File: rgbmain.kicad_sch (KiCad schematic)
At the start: 6 parts, among them J1 Conn_01x10_Pin, J2 Conn_01x10_Pin, J3 Conn_01x09_Pin, J4 Conn_01x09_Pin, J5 Conn_01x06_Pin, J6 Conn_01x06_Pin

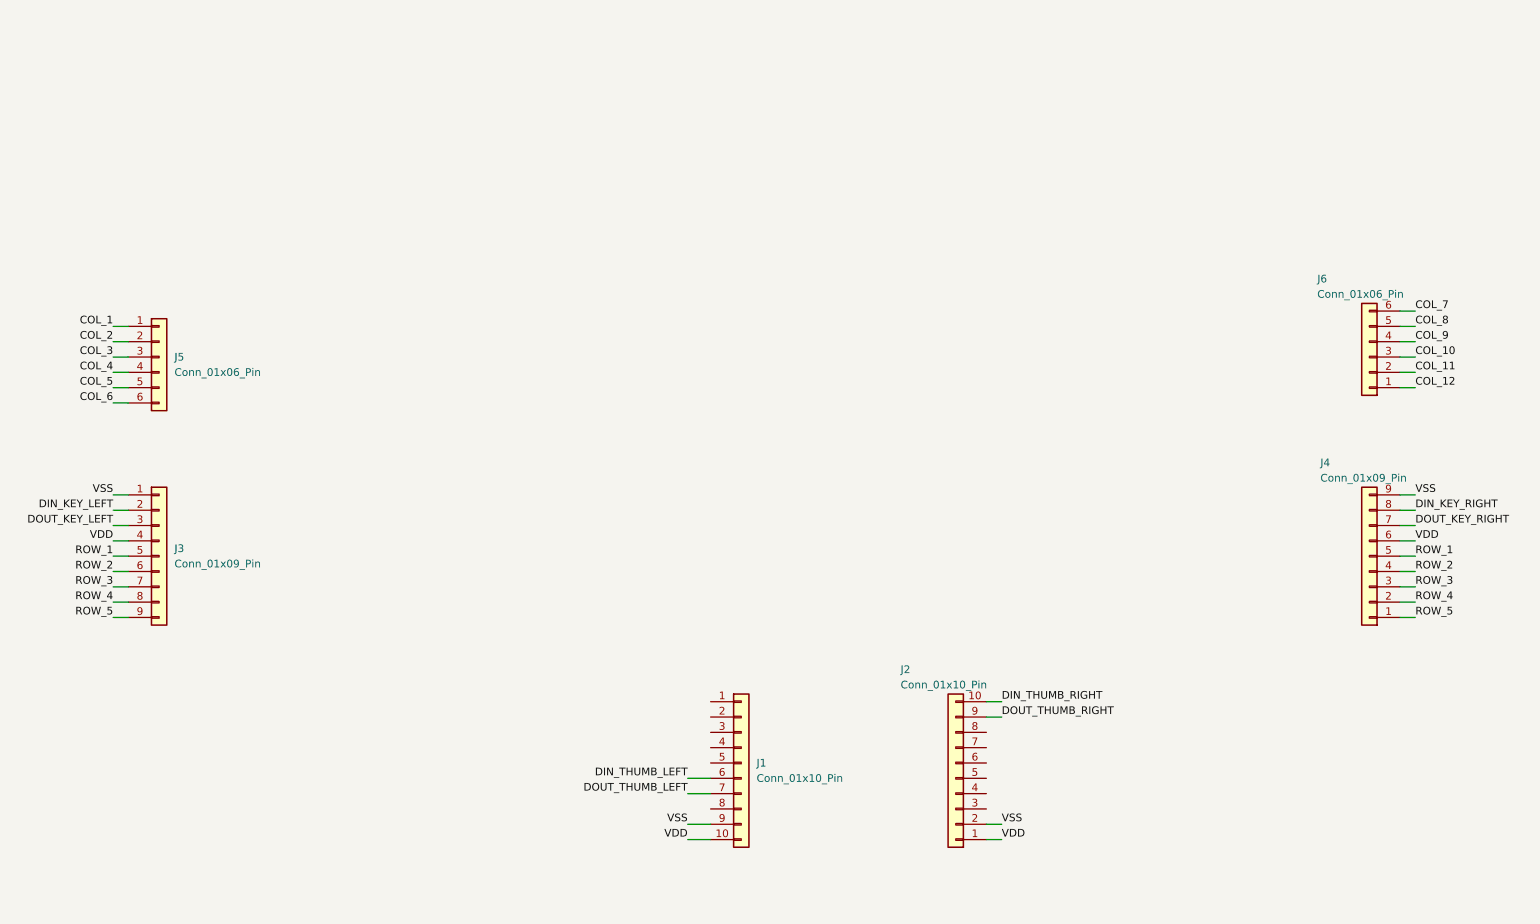
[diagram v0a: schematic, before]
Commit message: right side connectors were rotated incorrectly
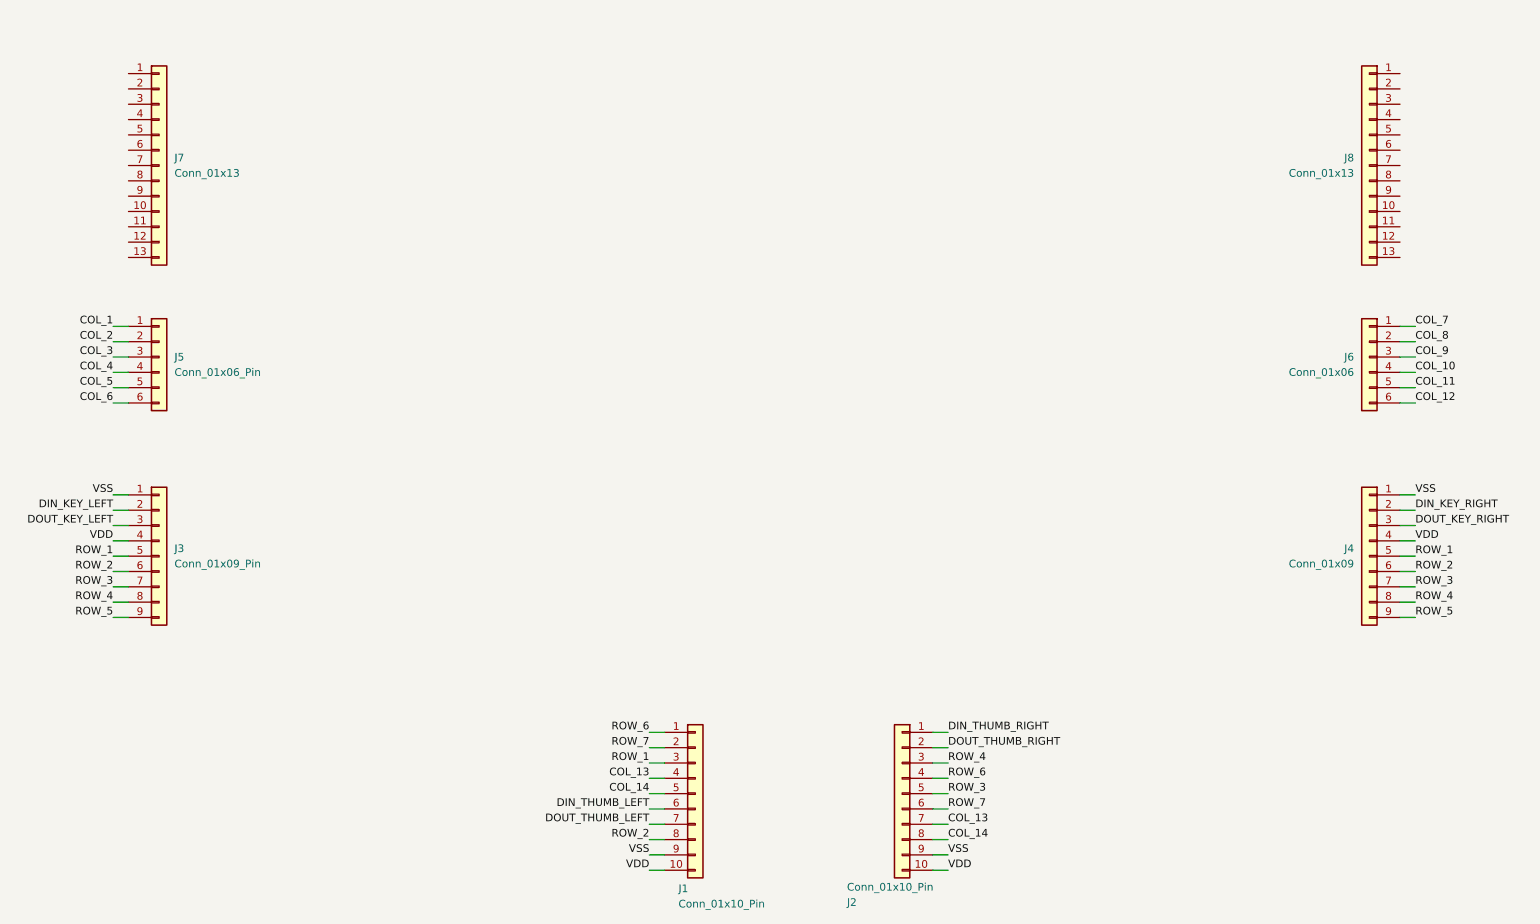
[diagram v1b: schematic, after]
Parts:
- added J7, J8: Conn_01x13, symbol Connector_Generic:Conn_01x13
- J4: value Conn_01x09_Pin -> Conn_01x09
- J6: value Conn_01x06_Pin -> Conn_01x06
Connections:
- net COL_10: now also J6.4 (Pin_4); no longer J6.3 (Pin_3)
- net COL_11: now also J6.5 (Pin_5); no longer J6.2 (Pin_2)
- net COL_12: now also J6.6 (Pin_6); no longer J6.1 (Pin_1)
- net COL_7: now also J6.1 (Pin_1); no longer J6.6 (Pin_6)
- net COL_8: now also J6.2 (Pin_2); no longer J6.5 (Pin_5)
- net COL_9: now also J6.3 (Pin_3); no longer J6.4 (Pin_4)
- net DIN_KEY_RIGHT: now also J4.2 (Pin_2); no longer J4.8 (Pin_8)
- net DIN_THUMB_RIGHT: now also J2.1 (Pin_1); no longer J2.10 (Pin_10)
- net DOUT_KEY_RIGHT: now also J4.3 (Pin_3); no longer J4.7 (Pin_7)
- net DOUT_THUMB_RIGHT: now also J2.2 (Pin_2); no longer J2.9 (Pin_9)
- net ROW_1: now also J1.3 (Pin_3)
- net ROW_2: now also J1.8 (Pin_8), J4.6 (Pin_6); no longer J4.4 (Pin_4)
- net ROW_3: now also J2.5 (Pin_5), J4.7 (Pin_7); no longer J4.3 (Pin_3)
- net ROW_4: now also J2.3 (Pin_3), J4.8 (Pin_8); no longer J4.2 (Pin_2)
- net ROW_5: now also J4.9 (Pin_9); no longer J4.1 (Pin_1)
- net VDD: now also J2.10 (Pin_10), J4.4 (Pin_4); no longer J2.1 (Pin_1), J4.6 (Pin_6)
- net VSS: now also J2.9 (Pin_9), J4.1 (Pin_1); no longer J2.2 (Pin_2), J4.9 (Pin_9)
- net ROW_6: now reaches J2.4 (Pin_4)
- net ROW_6: now also J1.1 (Pin_1)
- net ROW_7: now reaches J2.6 (Pin_6)
- net ROW_7: now also J1.2 (Pin_2)
- net COL_13: now reaches J2.7 (Pin_7)
- net COL_13: now also J1.4 (Pin_4)
- net COL_14: now reaches J2.8 (Pin_8)
- net COL_14: now also J1.5 (Pin_5)
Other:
- moved on the sheet: J1, J2

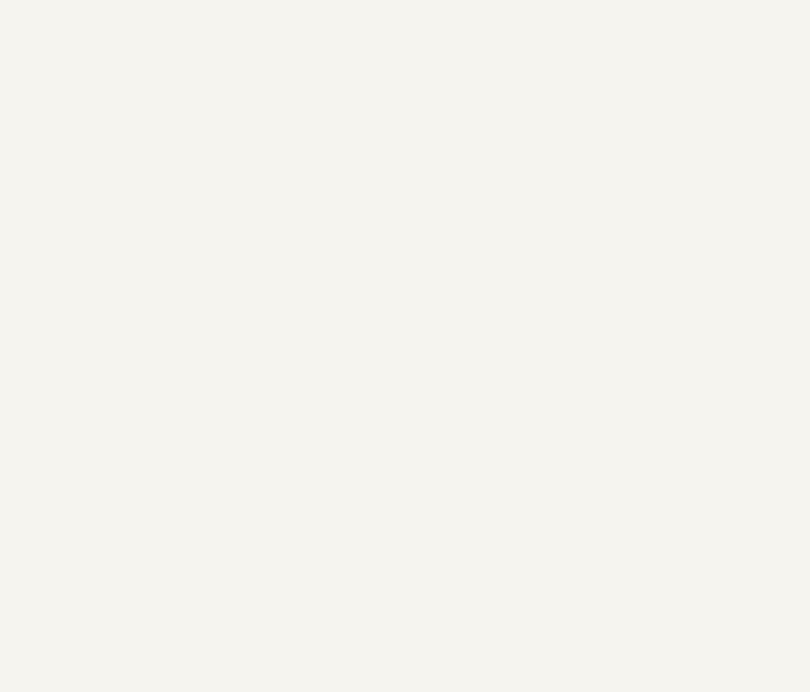
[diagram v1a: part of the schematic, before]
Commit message: symbol for Elite-Pi added
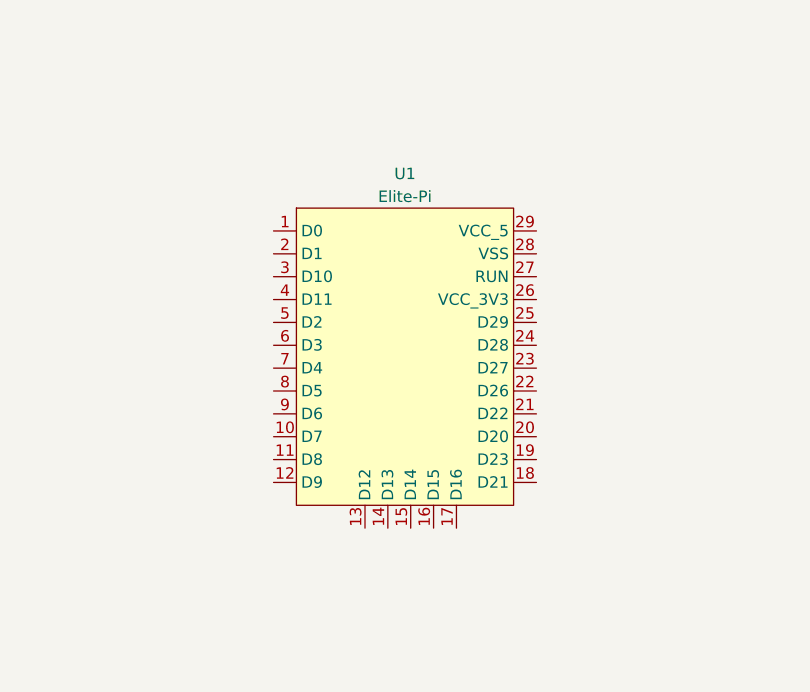
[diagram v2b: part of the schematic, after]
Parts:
- added U1: Elite-Pi, symbol rgbmain:Elite-PI
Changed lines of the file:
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@@
+	)
+	(symbol
+		(lib_id "rgbmain:Elite-PI")
+		(at 144.78 62.23 0)
+		(unit 1)
+		(exclude_from_sim no)
+		(in_bom yes)
+		(on_board yes)
+		(dnp no)
+		(fields_autoplaced yes)
+		(property "Reference" "U1"
+			(at 144.145 43.18 0)
+			(effects
+				(font
+					(size 1.27 1.27)
+				)
+			)
+		)
+		(property "Value" "Elite-Pi"
+			(at 144.145 45.72 0)
+			(effects
+				(font
+					(size 1.27 1.27)
+				)
+			)
+		)
+		(property "Footprint" ""
+			(at 144.78 62.23 0)
+			(effects
+				(font
+					(size 1.27 1.27)
+				)
+			)
+		)
+		(property "Datasheet" "https://docs.keeb.io/elite-pi-guide"
+			(at 144.526 97.536 0)
+			(effects
+				(font
+					(size 1.27 1.27)
+				)
+				(hide yes)
+			)
+		)
+		(property "Description" "Elite-Pi is a microcontroller based on the RP2040 designed for custom keyboards."
+			(at 144.526 95.504 0)
+			(effects
+				(font
+					(size 1.27 1.27)
+				)
+				(hide yes)
+			)
+		)
+		(pin "19"
+		)
+		(pin "15"
+		)
+		(pin "17"
+		)
+		(pin "22"
+		)
+		(pin "21"
+		)
+		(pin "12"
+		)
+		(pin "7"
+		)
+		(pin "18"
+		)
+		(pin "5"
+		)
+		(pin "16"
+		)
+		(pin "13"
+		)
+		(pin "8"
+		)
+		(pin "26"
+		)
+		(pin "14"
+		)
+		(pin "24"
+		)
+		(pin "10"
+		)
+		(pin "6"
+		)
+		(pin "3"
+		)
+		(pin "20"
+		)
+		(pin "23"
+		)
+		(pin "29"
+		)
+		(pin "9"
+		)
+		(pin "25"
+		)
+		(pin "1"
+		)
+		(pin "4"
+		)
+		(pin "11"
+		)
+		(pin "27"
+		)
+		(pin "28"
+		)
+		(pin "2"
+		)
+		(instances
+			(project ""
+				(path "/24ca604d-a7a4-46c7-a288-45b7cfc45cc9"
+					(reference "U1")
+					(unit 1)
+				)
+			)
+		)
 	)
 	(symbol

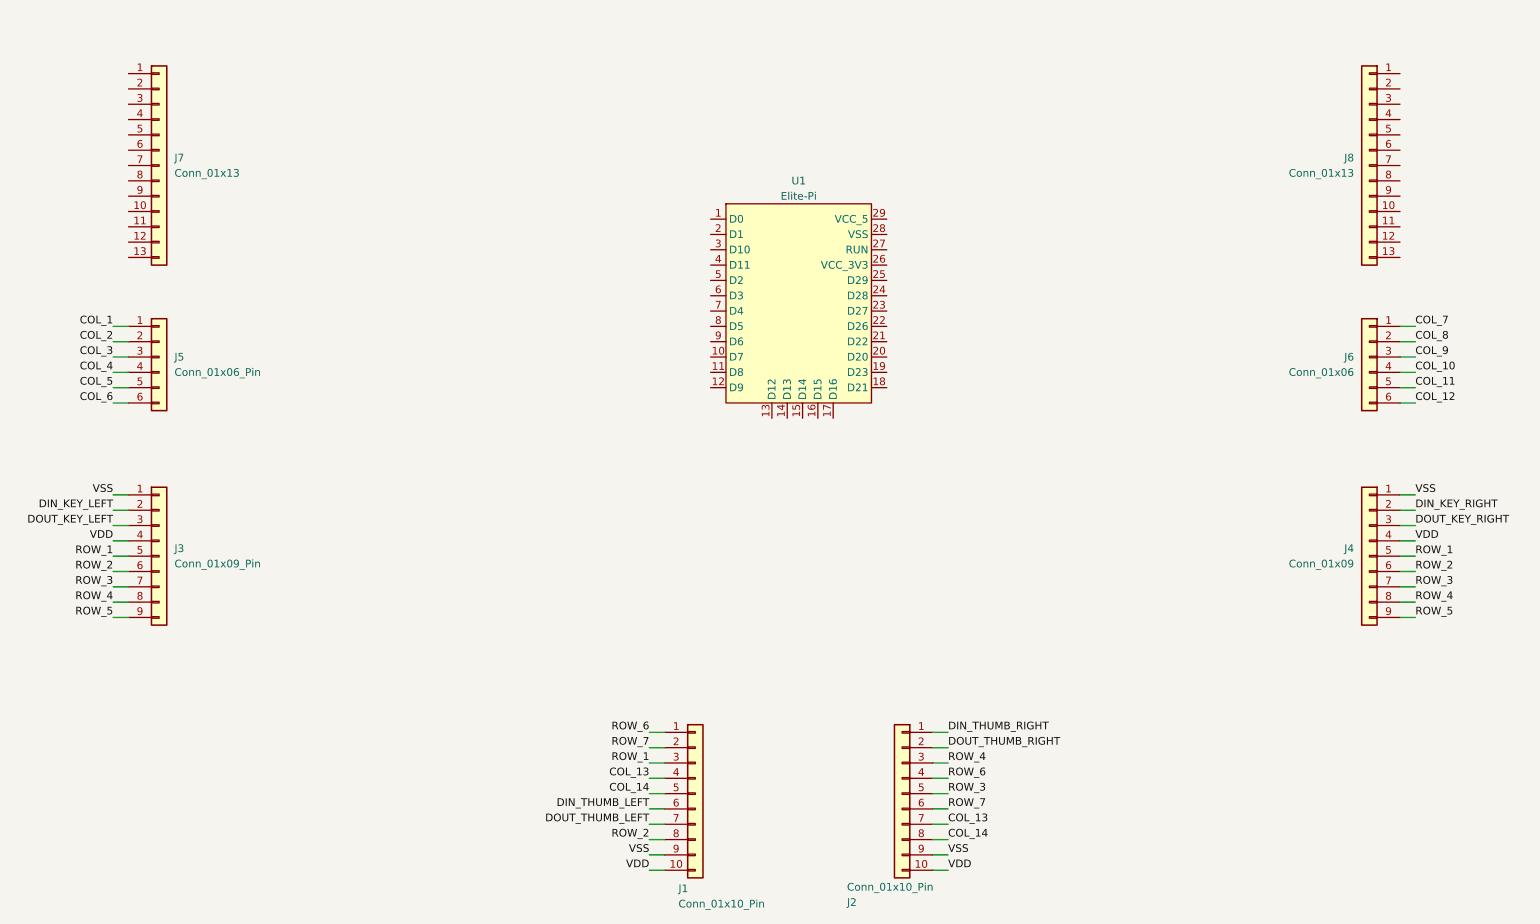
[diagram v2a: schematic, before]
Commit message: wire mcu up
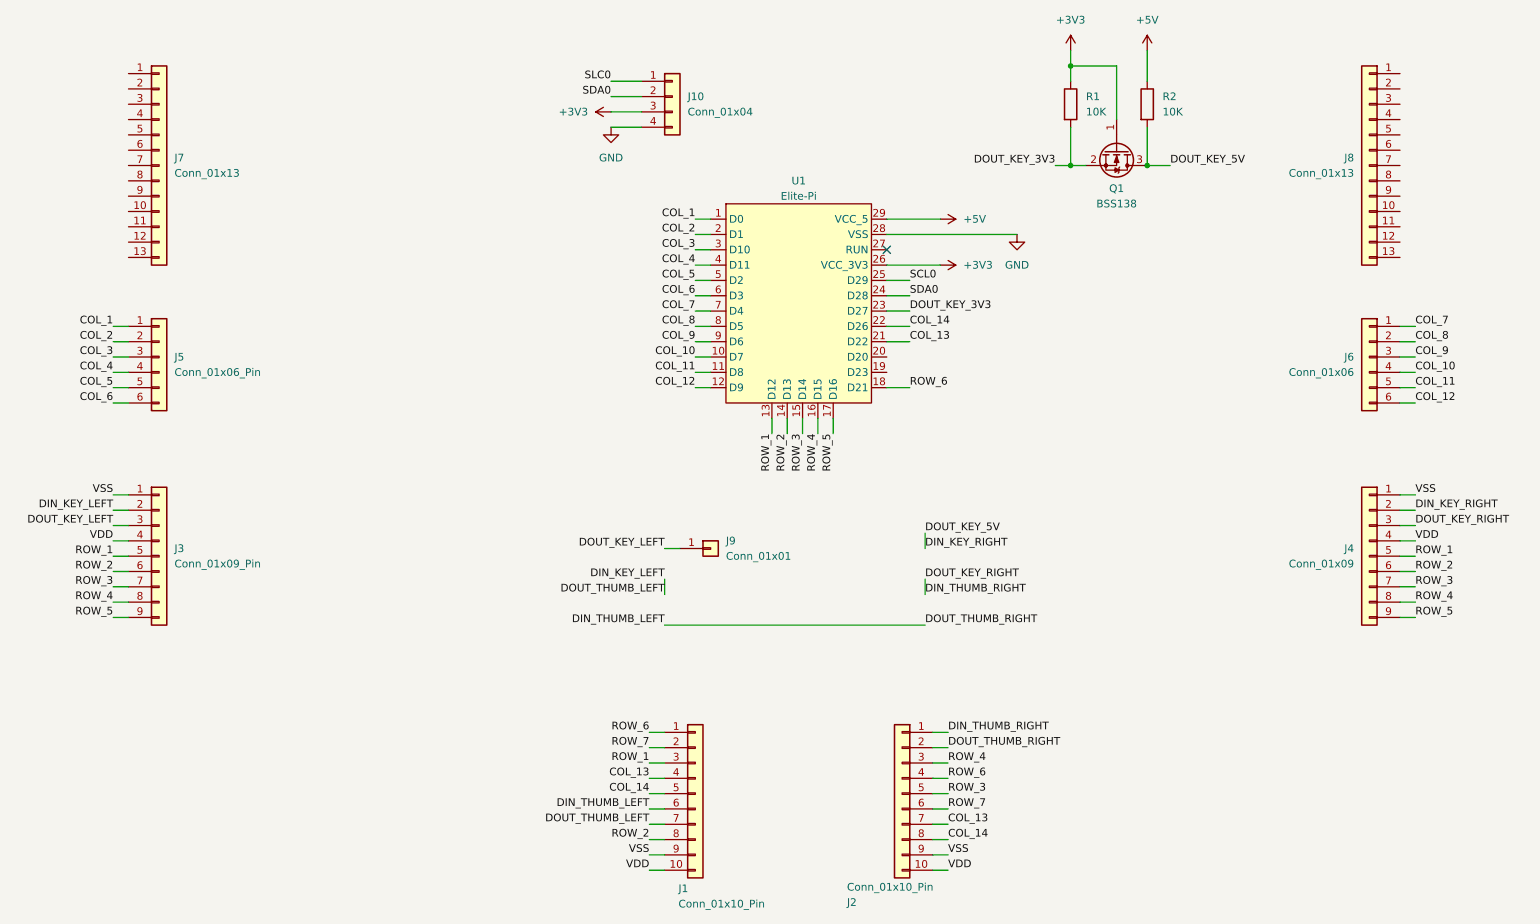
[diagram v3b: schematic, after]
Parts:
- added J10: Conn_01x04, symbol Connector_Generic:Conn_01x04
- added J9: Conn_01x01, symbol Connector_Generic:Conn_01x01
- added Q1: BSS138, Package_TO_SOT_SMD:SOT-23, symbol Transistor_FET:BSS138
- added R1, R2: 10K, symbol Device:R
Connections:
- net DOUT_KEY_RIGHT is gone; now on net DIN_THUMB_RIGHT: J4.3 (Pin_3)
- net DOUT_THUMB_LEFT is gone; now on net DIN_KEY_LEFT: J1.7 (Pin_7)
- net DOUT_THUMB_RIGHT is gone; now on net DIN_THUMB_LEFT: J2.2 (Pin_2)
- net COL_1: now also U1.1 (D0)
- net COL_10: now also U1.10 (D7)
- net COL_11: now also U1.11 (D8)
- net COL_12: now also U1.12 (D9)
- net COL_13: now also U1.21 (D22)
- net COL_14: now also U1.22 (D26)
- net COL_2: now also U1.2 (D1)
- net COL_3: now also U1.3 (D10)
- net COL_4: now also U1.4 (D11)
- net COL_5: now also U1.5 (D2)
- net COL_6: now also U1.6 (D3)
- net COL_7: now also U1.7 (D4)
- net COL_8: now also U1.8 (D5)
- net COL_9: now also U1.9 (D6)
- net DIN_KEY_RIGHT: now also Q1.3 (D), R2.2
- net DOUT_KEY_LEFT: now also J9.1 (Pin_1)
- net ROW_1: now also U1.13 (D12)
- net ROW_2: now also U1.14 (D13)
- net ROW_3: now also U1.15 (D14)
- net ROW_4: now also U1.16 (D15)
- net ROW_5: now also U1.17 (D16)
- net ROW_6: now also U1.18 (D21)
- net DOUT_KEY_3V3: now reaches U1.23 (D27)
- net DOUT_KEY_3V3: now also Q1.2 (S), R1.2
- net SDA0: now reaches U1.24 (D28)
- net SDA0: now also J10.2 (Pin_2)
- net SCL0: now reaches U1.25 (D29)
- net +3V3: now reaches U1.26 (VCC_3V3)
- net +3V3: now also J10.3 (Pin_3), Q1.1 (G), R1.1
- net GND: now reaches U1.28 (VSS)
- net GND: now also J10.4 (Pin_4)
- net +5V: now reaches U1.29 (VCC_5)
- net +5V: now also R2.1
- new net SLC0: J10.1 (Pin_1)
- no-connect marks 0 -> 1

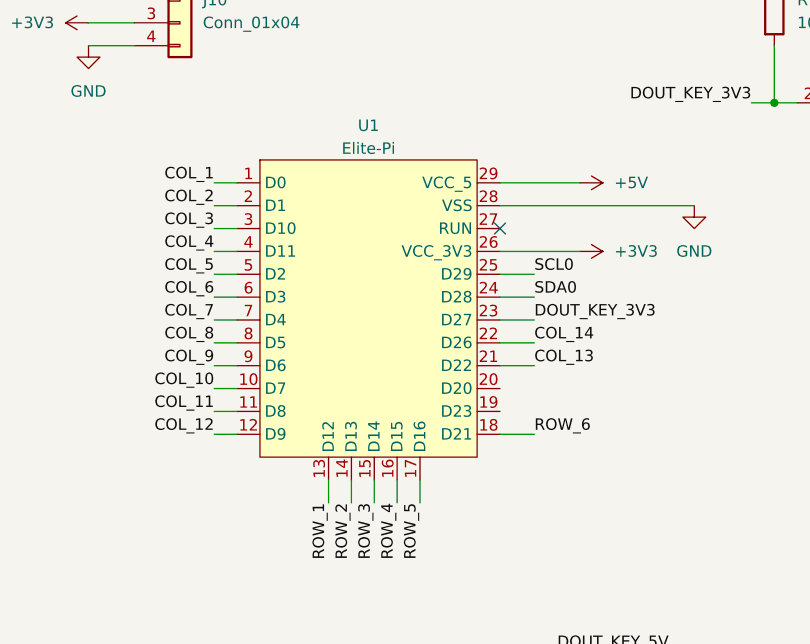
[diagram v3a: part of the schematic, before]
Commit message: changed number to match footprint
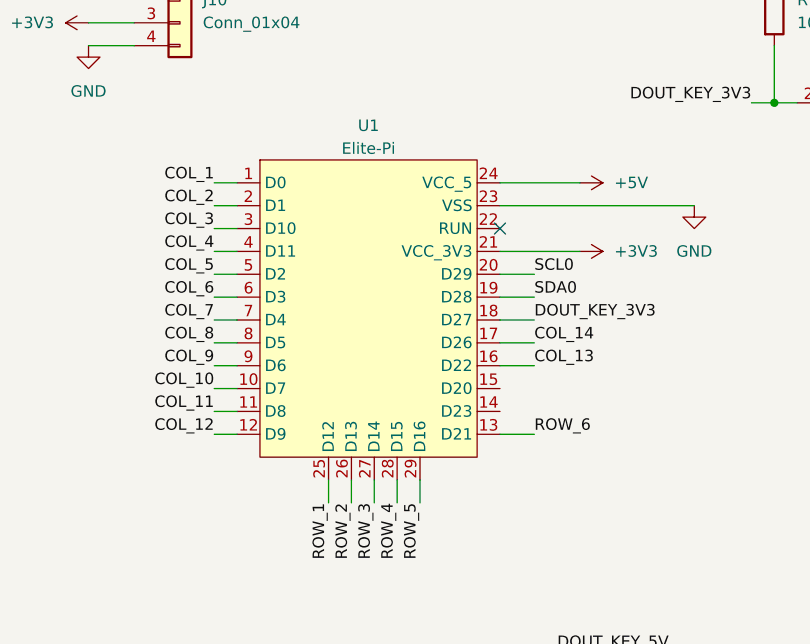
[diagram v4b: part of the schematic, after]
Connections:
- net +3V3: now also U1.21 (VCC_3V3); no longer U1.26 (VCC_3V3)
- net +5V: now also U1.24 (VCC_5); no longer U1.29 (VCC_5)
- net COL_13: now also U1.16 (D22); no longer U1.21 (D22)
- net COL_14: now also U1.17 (D26); no longer U1.22 (D26)
- net DOUT_KEY_3V3: now also U1.18 (D27); no longer U1.23 (D27)
- net GND: now also U1.23 (VSS); no longer U1.28 (VSS)
- net ROW_1: now also U1.25 (D12); no longer U1.13 (D12)
- net ROW_2: now also U1.26 (D13); no longer U1.14 (D13)
- net ROW_3: now also U1.27 (D14); no longer U1.15 (D14)
- net ROW_4: now also U1.28 (D15); no longer U1.16 (D15)
- net ROW_5: now also U1.29 (D16); no longer U1.17 (D16)
- net ROW_6: now also U1.13 (D21); no longer U1.18 (D21)
- net SCL0: now also U1.20 (D29); no longer U1.25 (D29)
- net SDA0: now also U1.19 (D28); no longer U1.24 (D28)
